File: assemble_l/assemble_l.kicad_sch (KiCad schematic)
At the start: 57 parts, among them J1 Conn_01x02_Pin, SW1 SW_Push, SW10 SW_Push, SW11 SW_Push, SW12 SW_Push, SW13 SW_Push, SW14 SW_Push, SW15 SW_Push, SW16 SW_Push, SW17 SW_Push, SW18 SW_Push, SW19 SW_Push, SW2 SW_Push, SW20 SW_Push, SW21 SW_Push, SW22 SW_Push, SW23 SW_Push, SW24 SW_Push, SW25 SW_Push, SW26 SW_Push, SW27 SW_Push, SW28 SW_Push, SW3 SW_Push, SW4 SW_Push, SW5 SW_Push, SW6 SW_Push, SW7 SW_Push, SW8 SW_Push, SW9 SW_Push, U1 Micon_BLEMicroPro

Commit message: feat: implement left side
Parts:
- SW1, SW10, SW11, SW12, SW13, SW14, SW15, SW16, SW17, SW18, SW19, SW2, SW20, SW21, SW22, SW23, SW24, SW25, SW26, SW27, SW3, SW4, SW5, SW6, SW7, SW8, SW9: footprint kbd_SW:Choc_v2_Hotswap_1u -> kbd_SW:Choc_v2_Hotswap_1u_16.5
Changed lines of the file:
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@@
 			)
 		)
-		(property "Footprint" "kbd_SW:Choc_v2_Hotswap_1u"
+		(property "Footprint" "kbd_SW:Choc_v2_Hotswap_1u_16.5"
 			(at 132.08 146.05 0)
 			(effects
@@
 			)
 		)
-		(property "Footprint" "kbd_SW:Choc_v2_Hotswap_1u"
+		(property "Footprint" "kbd_SW:Choc_v2_Hotswap_1u_16.5"
 			(at 116.84 165.1 0)
 			(effects
@@
 			)
 		)
-		(property "Footprint" "kbd_SW:Choc_v2_Hotswap_1u"
+		(property "Footprint" "kbd_SW:Choc_v2_Hotswap_1u_16.5"
 			(at 148.59 124.46 0)
 			(effects
@@
 			)
 		)
-		(property "Footprint" "kbd_SW:Choc_v2_Hotswap_1u"
+		(property "Footprint" "kbd_SW:Choc_v2_Hotswap_1u_16.5"
 			(at 116.84 146.05 0)
 			(effects
@@
 			)
 		)
-		(property "Footprint" "kbd_SW:Choc_v2_Hotswap_1u"
+		(property "Footprint" "kbd_SW:Choc_v2_Hotswap_1u_16.5"
 			(at 93.98 124.46 0)
 			(effects
@@
 			)
 		)
-		(property "Footprint" "kbd_SW:Choc_v2_Hotswap_1u"
+		(property "Footprint" "kbd_SW:Choc_v2_Hotswap_1u_16.5"
 			(at 116.84 124.46 0)
 			(effects
@@
 			)
 		)
-		(property "Footprint" "kbd_SW:Choc_v2_Hotswap_1u"
+		(property "Footprint" "kbd_SW:Choc_v2_Hotswap_1u_16.5"
 			(at 116.84 107.95 0)
 			(effects
@@
 			)
 		)
-		(property "Footprint" "kbd_SW:Choc_v2_Hotswap_1u"
+		(property "Footprint" "kbd_SW:Choc_v2_Hotswap_1u_16.5"
 			(at 148.59 165.1 0)
 			(effects
@@
 			)
 		)
-		(property "Footprint" "kbd_SW:Choc_v2_Hotswap_1u"
+		(property "Footprint" "kbd_SW:Choc_v2_Hotswap_1u_16.5"
 			(at 55.88 124.46 0)
 			(effects
@@
 			)
 		)
-		(property "Footprint" "kbd_SW:Choc_v2_Hotswap_1u"
+		(property "Footprint" "kbd_SW:Choc_v2_Hotswap_1u_16.5"
 			(at 74.93 146.05 0)
 			(effects
@@
 			)
 		)
-		(property "Footprint" "kbd_SW:Choc_v2_Hotswap_1u"
+		(property "Footprint" "kbd_SW:Choc_v2_Hotswap_1u_16.5"
 			(at 55.88 88.9 0)
 			(effects
@@
 			)
 		)
-		(property "Footprint" "kbd_SW:Choc_v2_Hotswap_1u"
+		(property "Footprint" "kbd_SW:Choc_v2_Hotswap_1u_16.5"
 			(at 74.93 88.9 0)
 			(effects
@@
 			)
 		)
-		(property "Footprint" "kbd_SW:Choc_v2_Hotswap_1u"
+		(property "Footprint" "kbd_SW:Choc_v2_Hotswap_1u_16.5"
 			(at 132.08 88.9 0)
 			(effects
@@
 			)
 		)
-		(property "Footprint" "kbd_SW:Choc_v2_Hotswap_1u"
+		(property "Footprint" "kbd_SW:Choc_v2_Hotswap_1u_16.5"
 			(at 132.08 165.1 0)
 			(effects
@@
 			)
 		)
-		(property "Footprint" "kbd_SW:Choc_v2_Hotswap_1u"
+		(property "Footprint" "kbd_SW:Choc_v2_Hotswap_1u_16.5"
 			(at 93.98 88.9 0)
 			(effects
@@
 			)
 		)
-		(property "Footprint" "kbd_SW:Choc_v2_Hotswap_1u"
+		(property "Footprint" "kbd_SW:Choc_v2_Hotswap_1u_16.5"
 			(at 148.59 107.95 0)
 			(effects
@@
 			)
 		)
-		(property "Footprint" "kbd_SW:Choc_v2_Hotswap_1u"
+		(property "Footprint" "kbd_SW:Choc_v2_Hotswap_1u_16.5"
 			(at 55.88 107.95 0)
 			(effects
@@
 			)
 		)
-		(property "Footprint" "kbd_SW:Choc_v2_Hotswap_1u"
+		(property "Footprint" "kbd_SW:Choc_v2_Hotswap_1u_16.5"
 			(at 55.88 146.05 0)
 			(effects
@@
 			)
 		)
-		(property "Footprint" "kbd_SW:Choc_v2_Hotswap_1u"
+		(property "Footprint" "kbd_SW:Choc_v2_Hotswap_1u_16.5"
 			(at 74.93 124.46 0)
 			(effects
@@
 			)
 		)
-		(property "Footprint" "kbd_SW:Choc_v2_Hotswap_1u"
+		(property "Footprint" "kbd_SW:Choc_v2_Hotswap_1u_16.5"
 			(at 74.93 107.95 0)
 			(effects
@@
 			)
 		)
-		(property "Footprint" "kbd_SW:Choc_v2_Hotswap_1u"
+		(property "Footprint" "kbd_SW:Choc_v2_Hotswap_1u_16.5"
 			(at 93.98 107.95 0)
 			(effects
@@
 			)
 		)
-		(property "Footprint" "kbd_SW:Choc_v2_Hotswap_1u"
+		(property "Footprint" "kbd_SW:Choc_v2_Hotswap_1u_16.5"
 			(at 132.08 107.95 0)
 			(effects
@@
 			)
 		)
-		(property "Footprint" "kbd_SW:Choc_v2_Hotswap_1u"
+		(property "Footprint" "kbd_SW:Choc_v2_Hotswap_1u_16.5"
 			(at 132.08 124.46 0)
 			(effects
@@
 			)
 		)
-		(property "Footprint" "kbd_SW:Choc_v2_Hotswap_1u"
+		(property "Footprint" "kbd_SW:Choc_v2_Hotswap_1u_16.5"
 			(at 148.59 88.9 0)
 			(effects
@@
 			)
 		)
-		(property "Footprint" "kbd_SW:Choc_v2_Hotswap_1u"
+		(property "Footprint" "kbd_SW:Choc_v2_Hotswap_1u_16.5"
 			(at 148.59 146.05 0)
 			(effects
@@
 			)
 		)
-		(property "Footprint" "kbd_SW:Choc_v2_Hotswap_1u"
+		(property "Footprint" "kbd_SW:Choc_v2_Hotswap_1u_16.5"
 			(at 93.98 146.05 0)
 			(effects
@@
 			)
 		)
-		(property "Footprint" "kbd_SW:Choc_v2_Hotswap_1u"
+		(property "Footprint" "kbd_SW:Choc_v2_Hotswap_1u_16.5"
 			(at 116.84 88.9 0)
 			(effects

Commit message: fix: DRC error
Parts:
- J1: footprint kbd_Parts:Battery_BMP_2pin -> kbd_Parts:Battery_2pin
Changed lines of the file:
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@@
 			)
 		)
-		(property "Footprint" "kbd_Parts:Battery_BMP_2pin"
+		(property "Footprint" "kbd_Parts:Battery_2pin"
 			(at 180.34 58.42 0)
 			(effects

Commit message: feat: reallocate keys on left
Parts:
- removed D19, D20, D21, D22, D23, D24: D, kbd_Parts:Diode_TH_SMD, symbol Device:D
- removed SW19, SW20, SW21, SW22, SW23, SW24: SW_Push, kbd_SW:Choc_v2_Hotswap_1u_16.5, symbol Switch:SW_Push
- renumbered D4 to D10, D10 to D11, D16 to D12, D25 to D13, D5 to D14, D11 to D15, D17 to D16, D26 to D17, D6 to D18, D12 to D19, D7 to D2, D18 to D20, D27 to D21, D13 to D3, D2 to D4, D8 to D5, D14 to D6, D3 to D7, D9 to D8, D15 to D9, SW4 to SW10, SW10 to SW11, SW16 to SW12, SW25 to SW13, SW5 to SW14, SW11 to SW15, SW17 to SW16, SW26 to SW17, SW6 to SW18, SW12 to SW19, SW7 to SW2, SW18 to SW20, SW27 to SW21, SW28 to SW22, SW13 to SW3, SW2 to SW4, SW8 to SW5, SW14 to SW6, SW3 to SW7, SW9 to SW8, SW15 to SW9
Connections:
- net Row3: now also D13.1 (K), D17.1 (K), D21.1 (K)
- removed net Row4: D13.1 (K), D17.1 (K), D21.1 (K), U1.11 (B4/PIN11)
- no-connect marks 8 -> 9
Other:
- moved on the sheet: D13, D17, D21, SW13, SW17, SW21

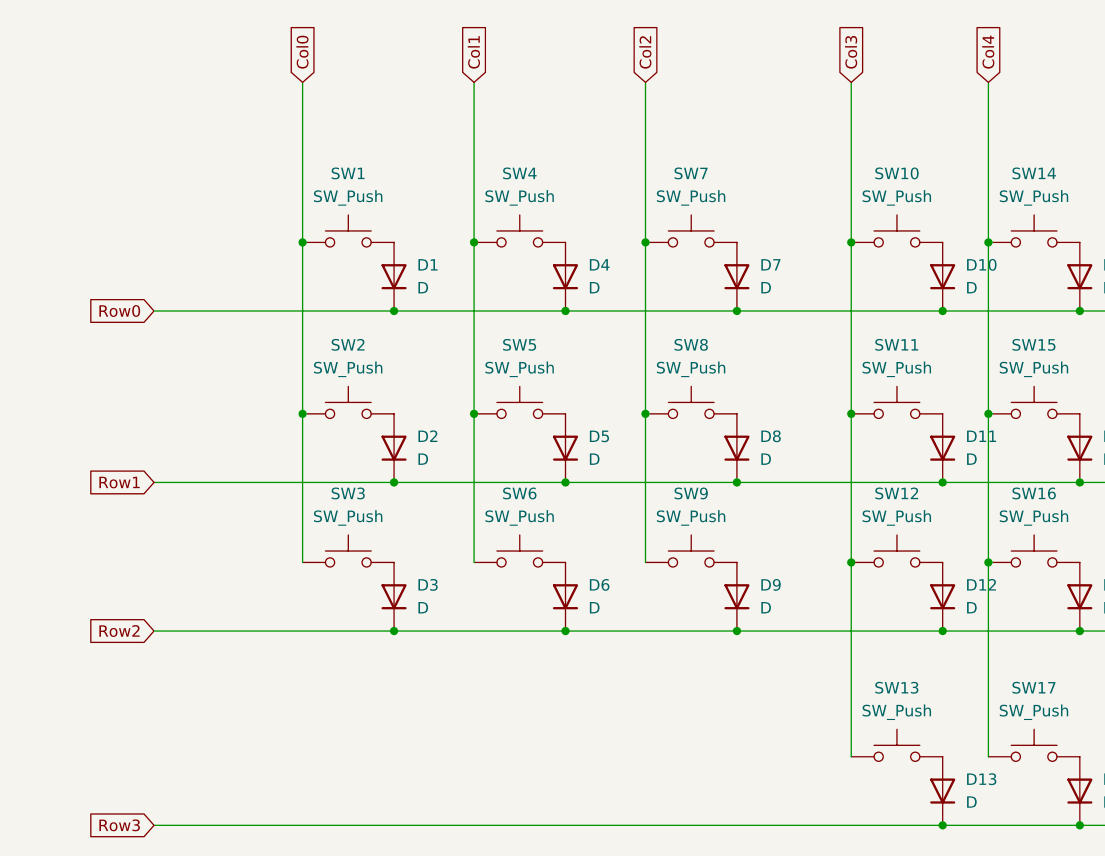
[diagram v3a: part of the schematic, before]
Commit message: feat: change key placement
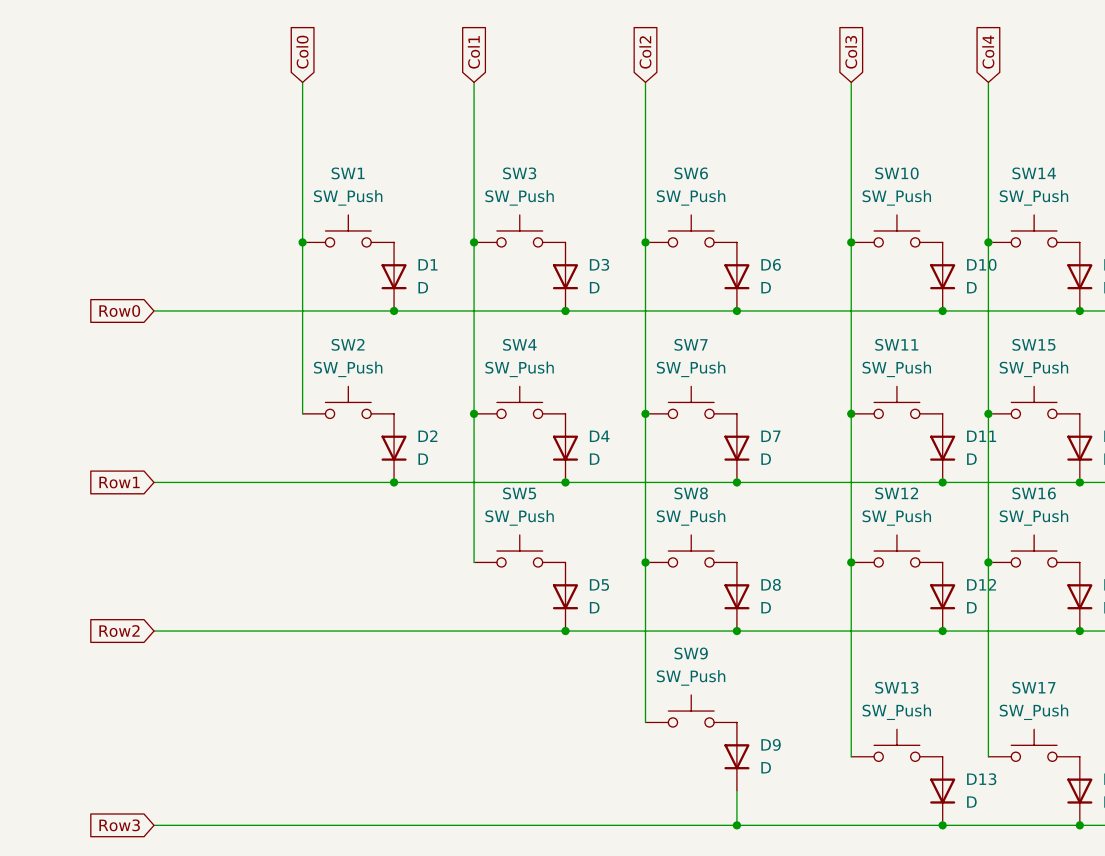
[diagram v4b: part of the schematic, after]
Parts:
- renumbered D4 to D3, D5 to D4, D6 to D5, D7 to D6, D8 to D7, D9 to D8, D3 to D9, SW4 to SW3, SW5 to SW4, SW6 to SW5, SW7 to SW6, SW8 to SW7, SW9 to SW8, SW3 to SW9
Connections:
- net Col0: no longer SW9.1
- net Col2: now also SW9.1
- net Row2: no longer D9.1 (K)
- net Row3: now also D9.1 (K)
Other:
- moved on the sheet: D9, SW9
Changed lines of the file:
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@@
 	)
 	(junction
-		(at 60.96 137.16)
-		(diameter 0)
-		(color 0 0 0 0)
-	)
-	(junction
 		(at 21.59 33.02)
 		(diameter 0)
@@
 	)
 	(junction
+		(at 99.06 158.75)
+		(diameter 0)
+		(color 0 0 0 0)
+	)
+	(junction
 		(at 137.16 158.75)
 		(diameter 0)
@@
 	)
 	(junction
-		(at 50.8 113.03)
+		(at 88.9 129.54)
 		(diameter 0)
 		(color 0 0 0 0)
@@
 	(wire
 		(pts
-			(xy 34.29 137.16) (xy 60.96 137.16)
+			(xy 34.29 137.16) (xy 80.01 137.16)
 		)
 		(stroke
@@
 	(wire
 		(pts
-			(xy 34.29 158.75) (xy 121.92 158.75)
-		)
-		(stroke
-			(width 0)
-			(type default)
-		)
-	)
-	(wire
-		(pts
-			(xy 88.9 113.03) (xy 88.9 129.54)
+			(xy 34.29 158.75) (xy 99.06 158.75)
 		)
 		(stroke
@@
 	(wire
 		(pts
-			(xy 60.96 137.16) (xy 80.01 137.16)
+			(xy 88.9 129.54) (xy 88.9 147.32)
 		)
 		(stroke
@@
 	(wire
 		(pts
-			(xy 50.8 113.03) (xy 50.8 129.54)
+			(xy 88.9 113.03) (xy 88.9 129.54)
 		)
 		(stroke
@@
 	(wire
 		(pts
+			(xy 99.06 158.75) (xy 121.92 158.75)
+		)
+		(stroke
+			(width 0)
+			(type default)
+		)
+	)
+	(wire
+		(pts
 			(xy 50.8 93.98) (xy 50.8 113.03)
 		)
@@
 	(wire
 		(pts
+			(xy 99.06 154.94) (xy 99.06 158.75)
+		)
+		(stroke
+			(width 0)
+			(type default)
+		)
+	)
+	(wire
+		(pts
 			(xy 60.96 101.6) (xy 80.01 101.6)
 		)
@@
 		(dnp no)
 		(fields_autoplaced yes)
-		(property "Reference" "SW9"
+		(property "Reference" "SW8"
 			(at 93.98 121.92 0)
 			(effects
@@
 			(project "wikbd_assemble_l"
 				(path "/d117cd26-8e7e-4c35-b450-26176f9e2abc"
-					(reference "SW9")
+					(reference "SW8")
 					(unit 1)
 				)
@@
 	(symbol
 		(lib_id "Switch:SW_Push")
-		(at 55.88 129.54 0)
+		(at 93.98 147.32 0)
 		(unit 1)
 		(exclude_from_sim no)
@@
 		(dnp no)
 		(fields_autoplaced yes)
-		(property "Reference" "SW3"
-			(at 55.88 121.92 0)
+		(property "Reference" "SW9"
+			(at 93.98 139.7 0)
 			(effects
 				(font
@@
 		)
 		(property "Value" "SW_Push"
-			(at 55.88 124.46 0)
+			(at 93.98 142.24 0)
 			(effects
 				(font
@@
 		)
 		(property "Footprint" "kbd_SW:Choc_v2_Hotswap_1u_16.5"
-			(at 55.88 124.46 0)
+			(at 93.98 142.24 0)
 			(effects
 				(font
@@
 		)
 		(property "Datasheet" "~"
-			(at 55.88 124.46 0)
+			(at 93.98 142.24 0)
 			(effects
 				(font
@@
 		)
 		(property "Description" "Push button switch, generic, two pins"
-			(at 55.88 129.54 0)
+			(at 93.98 147.32 0)
 			(effects
 				(font
@@
 			(project "wikbd_assemble_l"
 				(path "/d117cd26-8e7e-4c35-b450-26176f9e2abc"
-					(reference "SW3")
+					(reference "SW9")
 					(unit 1)
 				)
@@
 		(dnp no)
 		(fields_autoplaced yes)
-		(property "Reference" "D9"
+		(property "Reference" "D8"
 			(at 101.6 132.0799 90)
 			(effects
@@
 			(project "wikbd_assemble_l"
 				(path "/d117cd26-8e7e-4c35-b450-26176f9e2abc"
-					(reference "D9")
+					(reference "D8")
 					(unit 1)
 				)
@@
 		(dnp no)
 		(fields_autoplaced yes)
-		(property "Reference" "D7"
+		(property "Reference" "D6"
 			(at 101.6 96.5199 90)
 			(effects
@@
 			(project "wikbd_assemble_l"
 				(path "/d117cd26-8e7e-4c35-b450-26176f9e2abc"
-					(reference "D7")
+					(reference "D6")
 					(unit 1)
 				)
@@
 		(dnp no)
 		(fields_autoplaced yes)
-		(property "Reference" "D6"
+		(property "Reference" "D5"
 			(at 82.55 132.0799 90)
 			(effects
@@
 			(project "wikbd_assemble_l"
 				(path "/d117cd26-8e7e-4c35-b450-26176f9e2abc"
-					(reference "D6")
+					(reference "D5")
 					(unit 1)
 				)
@@
 		(dnp no)
 		(fields_autoplaced yes)
-		(property "Reference" "SW4"
+		(property "Reference" "SW3"
 			(at 74.93 86.36 0)
 			(effects
@@
 			(project "wikbd_assemble_l"
 				(path "/d117cd26-8e7e-4c35-b450-26176f9e2abc"
-					(reference "SW4")
+					(reference "SW3")
 					(unit 1)
 				)
@@
 		(dnp no)
 		(fields_autoplaced yes)
-		(property "Reference" "SW7"
+		(property "Reference" "SW6"
 			(at 93.98 86.36 0)
 			(effects
@@
 			(project "wikbd_assemble_l"
 				(path "/d117cd26-8e7e-4c35-b450-26176f9e2abc"
-					(reference "SW7")
+					(reference "SW6")
 					(unit 1)
 				)
@@
 	(symbol
 		(lib_id "Device:D")
-		(at 60.96 133.35 90)
+		(at 99.06 151.13 90)
 		(unit 1)
 		(exclude_from_sim no)
@@
 		(dnp no)
 		(fields_autoplaced yes)
-		(property "Reference" "D3"
-			(at 63.5 132.0799 90)
+		(property "Reference" "D9"
+			(at 101.6 149.8599 90)
 			(effects
 				(font
@@
 		)
 		(property "Value" "D"
-			(at 63.5 134.6199 90)
+			(at 101.6 152.3999 90)
 			(effects
 				(font
@@
 		)
 		(property "Footprint" "kbd_Parts:Diode_TH_SMD"
-			(at 60.96 133.35 0)
+			(at 99.06 151.13 0)
 			(effects
 				(font
@@
 		)
 		(property "Datasheet" "~"
-			(at 60.96 133.35 0)
+			(at 99.06 151.13 0)
 			(effects
 				(font
@@
 		)
 		(property "Description" "Diode"
-			(at 60.96 133.35 0)
+			(at 99.06 151.13 0)
 			(effects
 				(font
@@
 		)
 		(property "Sim.Device" "D"
-			(at 60.96 133.35 0)
+			(at 99.06 151.13 0)
 			(effects
 				(font
@@
 		)
 		(property "Sim.Pins" "1=K 2=A"
-			(at 60.96 133.35 0)
+			(at 99.06 151.13 0)
 			(effects
 				(font
@@
 			(project "wikbd_assemble_l"
 				(path "/d117cd26-8e7e-4c35-b450-26176f9e2abc"
-					(reference "D3")
+					(reference "D9")
 					(unit 1)
 				)
@@
 		(dnp no)
 		(fields_autoplaced yes)
-		(property "Reference" "SW6"
+		(property "Reference" "SW5"
 			(at 74.93 121.92 0)
 			(effects
@@
 			(project "wikbd_assemble_l"
 				(path "/d117cd26-8e7e-4c35-b450-26176f9e2abc"
-					(reference "SW6")
+					(reference "SW5")
 					(unit 1)
 				)
@@
 		(dnp no)
 		(fields_autoplaced yes)
-		(property "Reference" "SW5"
+		(property "Reference" "SW4"
 			(at 74.93 105.41 0)
 			(effects
@@
 			(project "wikbd_assemble_l"
 				(path "/d117cd26-8e7e-4c35-b450-26176f9e2abc"
-					(reference "SW5")
+					(reference "SW4")
 					(unit 1)
 				)
@@
 		(dnp no)
 		(fields_autoplaced yes)
-		(property "Reference" "SW8"
+		(property "Reference" "SW7"
 			(at 93.98 105.41 0)
 			(effects
@@
 			(project "wikbd_assemble_l"
 				(path "/d117cd26-8e7e-4c35-b450-26176f9e2abc"
-					(reference "SW8")
+					(reference "SW7")
 					(unit 1)
 				)
@@
 		(dnp no)
 		(fields_autoplaced yes)
-		(property "Reference" "D4"
+		(property "Reference" "D3"
 			(at 82.55 96.5199 90)
 			(effects
@@
 			(project "wikbd_assemble_l"
 				(path "/d117cd26-8e7e-4c35-b450-26176f9e2abc"
-					(reference "D4")
+					(reference "D3")
 					(unit 1)
 				)
@@
 		(dnp no)
 		(fields_autoplaced yes)
-		(property "Reference" "D8"
+		(property "Reference" "D7"
 			(at 101.6 115.5699 90)
 			(effects
@@
 			(project "wikbd_assemble_l"
 				(path "/d117cd26-8e7e-4c35-b450-26176f9e2abc"
-					(reference "D8")
+					(reference "D7")
 					(unit 1)
 				)
@@
 		(dnp no)
 		(fields_autoplaced yes)
-		(property "Reference" "D5"
+		(property "Reference" "D4"
 			(at 82.55 115.5699 90)
 			(effects
@@
 			(project "wikbd_assemble_l"
 				(path "/d117cd26-8e7e-4c35-b450-26176f9e2abc"
-					(reference "D5")
+					(reference "D4")
 					(unit 1)
 				)
